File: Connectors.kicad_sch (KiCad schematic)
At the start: 20 parts, among them J2 Conn_01x08_Male, J3 Conn_01x08_Male, J4 Conn_01x08_Male, J5 5V, J6 USB_C_Receptacle_USB2.0, U15 TPD4E02B04DQA

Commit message: плата практически готова
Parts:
- removed D?: D_Schottky, Diode_SMD:D_0603_1608Metric, symbol Device:D_Schottky
- J6: footprint (none) -> Connector_USB:USB_C_Receptacle_HRO_TYPE-C-31-M-12; Manufacturer_Part_Number (none) -> 918-418K2023S40001
- STM_DEBUG1: footprint Connector:Tag-Connect_TC2030-IDC-NL_2x03_P1.27mm_Vertical -> Connector:debug_port
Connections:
- net STM_DEBUG.SWCLK: now also STM_DEBUG1.4 (Pin_4); no longer STM_DEBUG1.5 (Pin_5)
- net STM_DEBUG.SWDIO: now also STM_DEBUG1.5 (Pin_5); no longer STM_DEBUG1.4 (Pin_4)
- net USB_BOARD.DN: now also U15.1 (IO1); no longer U15.4 (IO3)
- net USB_BOARD.DP: now also U15.2 (IO2); no longer U15.5 (IO4)
- net STM_DEBUG.3V3: now reaches STM_DEBUG1.6 (Pin_6)
- net PWR_IN1 renamed PWR_IN_CONN
- net PWR_IN2 renamed VBUS
- net VBUS: now also U15.5 (IO4); no longer U15.1 (IO1)
- net PWR_IN3 renamed PWR_IN_JST
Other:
- note added: "PWR"
- note added: "USB"
- moved on the sheet: J2, J3, J4, J5, J6, R38, R39, U15

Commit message: продам гараж
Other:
- moved on the sheet: CAM0, CAM1, J2, J3, J4, J5, LASER1, LED1, TELEM1, TELEM2

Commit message: )
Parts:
- removed LED1: Conn_01x03_Male, Connector_PinHeader_2.54mm:PinHeader_1x03_P2.54mm_Vertical, symbol Connector:Conn_01x03_Male
- added GND, LED: Conn_01x01_Male, TestPoint:TestPoint_Pad_D2.0mm, symbol Connector:Conn_01x01_Male
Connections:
- net GND: now also GND.1 (Pin_1)
- net RPI_GPIO21: now also LED.1 (Pin_1)
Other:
- moved on the sheet: J5, J6, POWER1, R38, R39, STM_DEBUG1, U15

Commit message: тестирование
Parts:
- GND1: renamed from GND; footprint TestPoint:TestPoint_Pad_D2.0mm -> TestPoint:TestPoint_Pad_D1.5mm
- LED1: renamed from LED; footprint TestPoint:TestPoint_Pad_D2.0mm -> TestPoint:TestPoint_Pad_D1.5mm
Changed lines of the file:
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@@
   (symbol (lib_id "Connector:Conn_01x01_Male") (at 149.86 106.68 0) (unit 1)
     (in_bom yes) (on_board yes)
-    (property "Reference" "LED" (id 0) (at 151.13 100.33 0))
+    (property "Reference" "LED1" (id 0) (at 151.13 100.33 0))
     (property "Value" "Conn_01x01_Male" (id 1) (at 151.13 103.1051 0))
-    (property "Footprint" "TestPoint:TestPoint_Pad_D2.0mm" (id 2) (at 149.86 106.68 0)
+    (property "Footprint" "TestPoint:TestPoint_Pad_D1.5mm" (id 2) (at 149.86 106.68 0)
       (effects (font (size 1.27 1.27)) hide)
     )
@@
   (symbol (lib_id "power:GND") (at 157.48 115.57 90) (mirror x) (unit 1)
     (in_bom yes) (on_board yes)
-    (property "Reference" "#PWR?" (id 0) (at 163.83 115.57 0)
+    (property "Reference" "#PWR0141" (id 0) (at 163.83 115.57 0)
       (effects (font (size 1.27 1.27)) hide)
     )
@@
   (symbol (lib_id "Connector:Conn_01x01_Male") (at 149.86 115.57 0) (unit 1)
     (in_bom yes) (on_board yes)
-    (property "Reference" "GND" (id 0) (at 151.13 109.22 0))
+    (property "Reference" "GND1" (id 0) (at 151.13 109.22 0))
     (property "Value" "Conn_01x01_Male" (id 1) (at 151.13 111.9951 0))
-    (property "Footprint" "TestPoint:TestPoint_Pad_D2.0mm" (id 2) (at 149.86 115.57 0)
+    (property "Footprint" "TestPoint:TestPoint_Pad_D1.5mm" (id 2) (at 149.86 115.57 0)
       (effects (font (size 1.27 1.27)) hide)
     )

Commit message: первый релиз
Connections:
- net STM_DEBUG.RX: now also STM_DEBUG1.2 (Pin_2); no longer STM_DEBUG1.3 (Pin_3)
- net STM_DEBUG.TX: now also STM_DEBUG1.3 (Pin_3); no longer STM_DEBUG1.2 (Pin_2)
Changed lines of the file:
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@@
     (effects (font (size 1.27 1.27)) (justify left bottom))
   )
-  (label "STM_DEBUG.TX" (at 25.4 127 0)
+  (label "STM_DEBUG.TX" (at 25.4 124.46 0)
     (effects (font (size 1.27 1.27)) (justify left bottom))
   )
@@
     (effects (font (size 1.27 1.27)) (justify left bottom))
   )
-  (label "STM_DEBUG.RX" (at 25.4 124.46 0)
+  (label "STM_DEBUG.RX" (at 25.4 127 0)
     (effects (font (size 1.27 1.27)) (justify left bottom))
   )

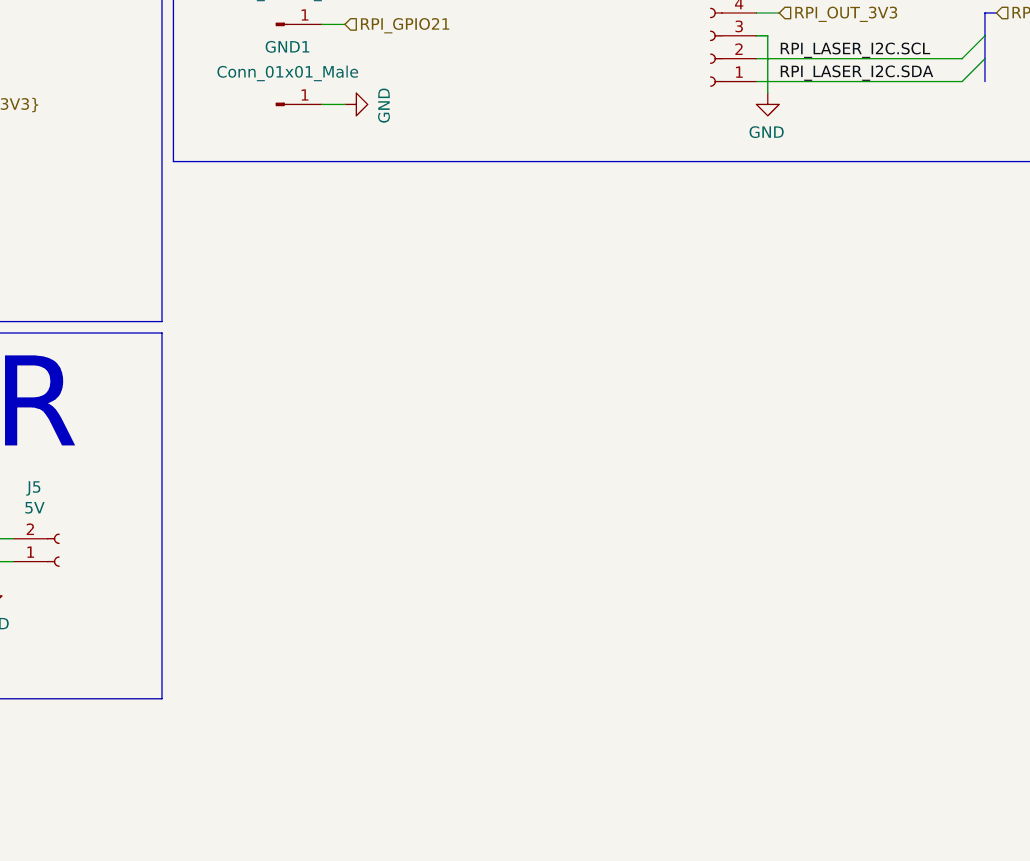
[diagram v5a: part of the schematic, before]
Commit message: Adding esp32 gpio pins
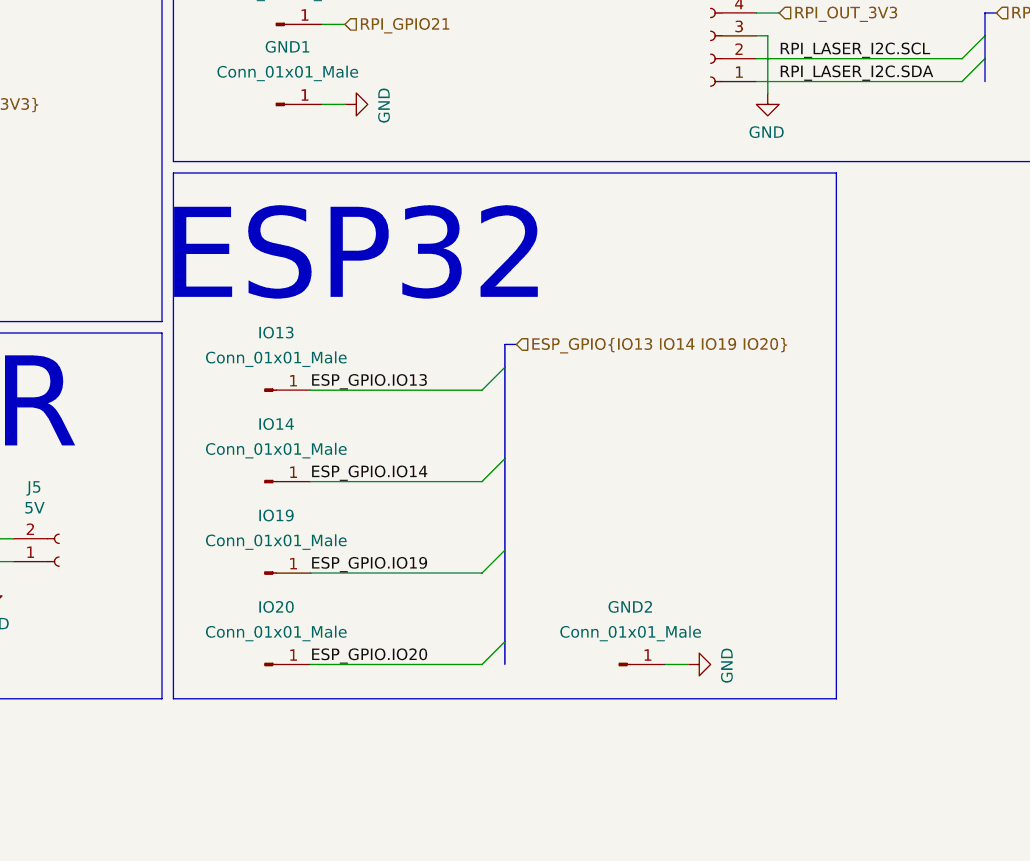
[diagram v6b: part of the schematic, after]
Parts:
- added GND2, IO13, IO14, IO19, IO20: Conn_01x01_Male, TestPoint:TestPoint_Pad_D1.5mm, symbol Connector:Conn_01x01_Male
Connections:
- net GND: now also GND2.1 (Pin_1)
- new net ESP_GPIO.IO13: IO13.1 (Pin_1)
- new net ESP_GPIO.IO14: IO14.1 (Pin_1)
- new net ESP_GPIO.IO19: IO19.1 (Pin_1)
- new net ESP_GPIO.IO20: IO20.1 (Pin_1)
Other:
- note added: "ESP32"
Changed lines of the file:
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@@
+    (stroke (width 0) (type default) (color 0 0 0 0))
+  )
+  (bus_entry (at 175.26 154.94) (size -2.54 2.54)
     (stroke (width 0) (type default) (color 0 0 0 0))
   )
@@
     (stroke (width 0) (type default) (color 0 0 0 0))
   )
+  (bus_entry (at 175.26 144.78) (size -2.54 2.54)
+    (stroke (width 0) (type default) (color 0 0 0 0))
+  )
   (bus_entry (at 226.06 40.64) (size -2.54 2.54)
     (stroke (width 0) (type default) (color 0 0 0 0))
@@
     (stroke (width 0) (type default) (color 0 0 0 0))
   )
+  (bus_entry (at 175.26 175.26) (size -2.54 2.54)
+    (stroke (width 0) (type default) (color 0 0 0 0))
+  )
   (bus_entry (at 48.26 116.84) (size -2.54 2.54)
     (stroke (width 0) (type default) (color 0 0 0 0))
@@
     (stroke (width 0) (type default) (color 0 0 0 0))
   )
+  (bus_entry (at 175.26 165.1) (size -2.54 2.54)
+    (stroke (width 0) (type default) (color 0 0 0 0))
+  )
   (bus_entry (at 102.87 33.02) (size -2.54 2.54)
     (stroke (width 0) (type default) (color 0 0 0 0))
@@
     (stroke (width 0) (type default) (color 0 0 0 0))
   )
+  (wire (pts (xy 193.04 177.8) (xy 195.58 177.8))
+    (stroke (width 0) (type default) (color 0 0 0 0))
+  )
+  (bus (pts (xy 175.26 144.78) (xy 175.26 154.94))
+    (stroke (width 0) (type default) (color 0 0 0 0))
+  )
   (bus (pts (xy 226.06 40.64) (xy 226.06 35.56))
     (stroke (width 0) (type default) (color 0 0 0 0))
@@
     (stroke (width 0) (type default) (color 0 0 0 0))
   )
+  (bus (pts (xy 175.26 165.1) (xy 175.26 175.26))
+    (stroke (width 0) (type default) (color 0 0 0 0))
+  )
   (bus (pts (xy 44.45 53.34) (xy 45.72 53.34))
     (stroke (width 0) (type default) (color 0 0 0 0))
@@
     (stroke (width 0) (type default) (color 0 0 0 0))
   )
+  (bus (pts (xy 175.26 154.94) (xy 175.26 165.1))
+    (stroke (width 0) (type default) (color 0 0 0 0))
+  )
   (bus (pts (xy 226.06 76.2) (xy 227.33 76.2))
     (stroke (width 0) (type default) (color 0 0 0 0))
@@
     (stroke (width 0) (type default) (color 0 0 0 0))
   )
+  (polyline (pts (xy 138.43 123.19) (xy 138.43 181.61))
+    (stroke (width 0) (type default) (color 0 0 0 0))
+  )
   (wire (pts (xy 151.13 71.12) (xy 153.67 71.12))
     (stroke (width 0) (type default) (color 0 0 0 0))
@@
     (stroke (width 0) (type default) (color 0 0 0 0))
   )
+  (polyline (pts (xy 212.09 181.61) (xy 212.09 123.19))
+    (stroke (width 0) (type default) (color 0 0 0 0))
+  )
   (polyline (pts (xy 12.7 139.7) (xy 12.7 12.7))
     (stroke (width 0) (type default) (color 0 0 0 0))
@@
     (stroke (width 0) (type default) (color 0 0 0 0))
   )
+  (polyline (pts (xy 212.09 123.19) (xy 138.43 123.19))
+    (stroke (width 0) (type default) (color 0 0 0 0))
+  )
   (polyline (pts (xy 138.43 121.92) (xy 251.46 121.92))
     (stroke (width 0) (type default) (color 0 0 0 0))
@@
     (stroke (width 0) (type default) (color 0 0 0 0))
   )
+  (bus (pts (xy 175.26 142.24) (xy 175.26 144.78))
+    (stroke (width 0) (type default) (color 0 0 0 0))
+  )
   (bus (pts (xy 114.3 92.71) (xy 114.3 95.25))
     (stroke (width 0) (type default) (color 0 0 0 0))
   )
+  (bus (pts (xy 176.53 142.24) (xy 175.26 142.24))
+    (stroke (width 0) (type default) (color 0 0 0 0))
+  )
   (bus (pts (xy 48.26 111.76) (xy 49.53 111.76))
     (stroke (width 0) (type default) (color 0 0 0 0))
@@
     (stroke (width 0) (type default) (color 0 0 0 0))
   )
+  (wire (pts (xy 153.67 147.32) (xy 172.72 147.32))
+    (stroke (width 0) (type default) (color 0 0 0 0))
+  )
   (bus (pts (xy 114.3 74.93) (xy 114.3 77.47))
     (stroke (width 0) (type default) (color 0 0 0 0))
@@
     (stroke (width 0) (type default) (color 0 0 0 0))
   )
+  (wire (pts (xy 153.67 167.64) (xy 172.72 167.64))
+    (stroke (width 0) (type default) (color 0 0 0 0))
+  )
   (bus (pts (xy 173.99 50.8) (xy 173.99 48.26))
     (stroke (width 0) (type default) (color 0 0 0 0))
@@
     (stroke (width 0) (type default) (color 0 0 0 0))
   )
+  (bus (pts (xy 175.26 175.26) (xy 175.26 177.8))
+    (stroke (width 0) (type default) (color 0 0 0 0))
+  )
   (wire (pts (xy 203.2 113.03) (xy 226.06 113.03))
     (stroke (width 0) (type default) (color 0 0 0 0))
@@
     (stroke (width 0) (type default) (color 0 0 0 0))
   )
+  (polyline (pts (xy 138.43 181.61) (xy 212.09 181.61))
+    (stroke (width 0) (type default) (color 0 0 0 0))
+  )
   (bus (pts (xy 173.99 35.56) (xy 173.99 33.02))
     (stroke (width 0) (type default) (color 0 0 0 0))
@@
     (stroke (width 0) (type default) (color 0 0 0 0))
   )
+  (wire (pts (xy 153.67 177.8) (xy 172.72 177.8))
+    (stroke (width 0) (type default) (color 0 0 0 0))
+  )
   (wire (pts (xy 41.91 179.07) (xy 41.91 181.61))
     (stroke (width 0) (type default) (color 0 0 0 0))
@@
   )
   (bus (pts (xy 173.99 55.88) (xy 173.99 50.8))
+    (stroke (width 0) (type default) (color 0 0 0 0))
+  )
+  (wire (pts (xy 153.67 157.48) (xy 172.72 157.48))
     (stroke (width 0) (type default) (color 0 0 0 0))
   )
@@
     (effects (font (size 10.0076 10.0076)) (justify left bottom))
   )
+  (text "ESP32" (at 137.16 138.43 0)
+    (effects (font (size 10.0076 10.0076)) (justify left bottom))
+  )
   (text "PWR" (at 96.52 154.94 0)
     (effects (font (size 10.0076 10.0076)) (justify left bottom))
   )
+  (label "ESP_GPIO.IO20" (at 153.67 177.8 0)
+    (effects (font (size 1.27 1.27)) (justify left bottom))
+  )
   (label "STM_ESC.CH8" (at 99.06 97.79 0)
     (effects (font (size 1.27 1.27)) (justify left bottom))
@@
     (effects (font (size 1.27 1.27)) (justify left bottom))
   )
+  (label "ESP_GPIO.IO14" (at 153.67 157.48 0)
+    (effects (font (size 1.27 1.27)) (justify left bottom))
+  )
   (label "STM_USART1.TX" (at 25.4 87.63 0)
     (effects (font (size 1.27 1.27)) (justify left bottom))
@@
     (effects (font (size 1.27 1.27)) (justify left bottom))
   )
+  (label "ESP_GPIO.IO19" (at 153.67 167.64 0)
+    (effects (font (size 1.27 1.27)) (justify left bottom))
+  )
   (label "STM_ESC.CH5" (at 99.06 90.17 0)
     (effects (font (size 1.27 1.27)) (justify left bottom))
@@
   )
   (label "STM_ESC.CH3" (at 99.06 85.09 0)
+    (effects (font (size 1.27 1.27)) (justify left bottom))
+  )
+  (label "ESP_GPIO.IO13" (at 153.67 147.32 0)
     (effects (font (size 1.27 1.27)) (justify left bottom))
   )
@@
   )
   (hierarchical_label "RPI_CAM0{CSI}" (shape input) (at 175.26 30.48 0)
+    (effects (font (size 1.27 1.27)) (justify left))
+  )
+  (hierarchical_label "ESP_GPIO{IO13 IO14 IO19 IO20}" (shape input) (at 176.53 142.24 0)
     (effects (font (size 1.27 1.27)) (justify left))
   )
@@
     (pin "2")
   )
+  (symbol (lib_id "Connector:Conn_01x01_Male") (at 148.59 157.48 0) (unit 1)
+    (in_bom yes) (on_board yes)
+    (property "Reference" "IO14" (id 0) (at 149.86 151.13 0))
+    (property "Value" "Conn_01x01_Male" (id 1) (at 149.86 153.9051 0))
+    (property "Footprint" "TestPoint:TestPoint_Pad_D1.5mm" (id 2) (at 148.59 157.48 0)
+      (effects (font (size 1.27 1.27)) hide)
+    )
+    (property "Datasheet" "~" (id 3) (at 148.59 157.48 0)
+      (effects (font (size 1.27 1.27)) hide)
+    )
+    (pin "1")
+  )
   (symbol (lib_id "Connector:USB_C_Receptacle_USB2.0") (at 26.67 181.61 0) (unit 1)
     (in_bom yes) (on_board yes) (fields_autoplaced)
@@
     (pin "S1")
   )
+  (symbol (lib_id "Connector:Conn_01x01_Male") (at 187.96 177.8 0) (unit 1)
+    (in_bom yes) (on_board yes)
+    (property "Reference" "GND2" (id 0) (at 189.23 171.45 0))
+    (property "Value" "Conn_01x01_Male" (id 1) (at 189.23 174.2251 0))
+    (property "Footprint" "TestPoint:TestPoint_Pad_D1.5mm" (id 2) (at 187.96 177.8 0)
+      (effects (font (size 1.27 1.27)) hide)
+    )
+    (property "Datasheet" "~" (id 3) (at 187.96 177.8 0)
+      (effects (font (size 1.27 1.27)) hide)
+    )
+    (pin "1")
+  )
+  (symbol (lib_id "Connector:Conn_01x01_Male") (at 148.59 147.32 0) (unit 1)
+    (in_bom yes) (on_board yes)
+    (property "Reference" "IO13" (id 0) (at 149.86 140.97 0))
+    (property "Value" "Conn_01x01_Male" (id 1) (at 149.86 143.7451 0))
+    (property "Footprint" "TestPoint:TestPoint_Pad_D1.5mm" (id 2) (at 148.59 147.32 0)
+      (effects (font (size 1.27 1.27)) hide)
+    )
+    (property "Datasheet" "~" (id 3) (at 148.59 147.32 0)
+      (effects (font (size 1.27 1.27)) hide)
+    )
+    (pin "1")
+  )
+  (symbol (lib_id "power:GND") (at 195.58 177.8 90) (mirror x) (unit 1)
+    (in_bom yes) (on_board yes)
+    (property "Reference" "#PWR0166" (id 0) (at 201.93 177.8 0)
+      (effects (font (size 1.27 1.27)) hide)
+    )
+    (property "Value" "GND" (id 1) (at 199.9742 177.927 0))
+    (property "Footprint" "" (id 2) (at 195.58 177.8 0)
+      (effects (font (size 1.27 1.27)) hide)
+    )
+    (property "Datasheet" "" (id 3) (at 195.58 177.8 0)
+      (effects (font (size 1.27 1.27)) hide)
+    )
+    (pin "1")
+  )
+  (symbol (lib_id "Connector:Conn_01x01_Male") (at 148.59 167.64 0) (unit 1)
+    (in_bom yes) (on_board yes)
+    (property "Reference" "IO19" (id 0) (at 149.86 161.29 0))
+    (property "Value" "Conn_01x01_Male" (id 1) (at 149.86 164.0651 0))
+    (property "Footprint" "TestPoint:TestPoint_Pad_D1.5mm" (id 2) (at 148.59 167.64 0)
+      (effects (font (size 1.27 1.27)) hide)
+    )
+    (property "Datasheet" "~" (id 3) (at 148.59 167.64 0)
+      (effects (font (size 1.27 1.27)) hide)
+    )
+    (pin "1")
+  )
+  (symbol (lib_id "Connector:Conn_01x01_Male") (at 148.59 177.8 0) (unit 1)
+    (in_bom yes) (on_board yes)
+    (property "Reference" "IO20" (id 0) (at 149.86 171.45 0))
+    (property "Value" "Conn_01x01_Male" (id 1) (at 149.86 174.2251 0))
+    (property "Footprint" "TestPoint:TestPoint_Pad_D1.5mm" (id 2) (at 148.59 177.8 0)
+      (effects (font (size 1.27 1.27)) hide)
+    )
+    (property "Datasheet" "~" (id 3) (at 148.59 177.8 0)
+      (effects (font (size 1.27 1.27)) hide)
+    )
+    (pin "1")
+  )
   (symbol (lib_id "power:GND") (at 118.11 168.91 0) (unit 1)

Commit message: Little fix
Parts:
- R38, R39: Manufacturer_Part_Number (none) -> 0402WGF5101TCE
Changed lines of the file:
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@@
+      (effects (font (size 1.27 1.27)) hide)
+    )
+    (property "Manufacturer_Part_Number" "0402WGF5101TCE" (id 4) (at 44.45 203.2 0)
       (effects (font (size 1.27 1.27)) hide)
     )
@@
       (effects (font (size 1.27 1.27)) hide)
     )
+    (property "Manufacturer_Part_Number" "0402WGF5101TCE" (id 4) (at 46.99 203.2 0)
+      (effects (font (size 1.27 1.27)) hide)
+    )

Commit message: First order
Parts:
- J5: Manufacturer_Part_Number XT30U-M -> (none)
- R38, R39: Manufacturer_Part_Number 0402WGF5101TCE -> PTFR0402B5K10N9
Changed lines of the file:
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@@
       (effects (font (size 1.27 1.27)) hide)
     )
-    (property "Manufacturer_Part_Number" "0402WGF5101TCE" (id 4) (at 44.45 203.2 0)
+    (property "Manufacturer_Part_Number" "PTFR0402B5K10N9" (id 4) (at 44.45 203.2 0)
       (effects (font (size 1.27 1.27)) hide)
     )
@@
       (effects (font (size 1.27 1.27)) hide)
     )
-    (property "Manufacturer_Part_Number" "0402WGF5101TCE" (id 4) (at 46.99 203.2 0)
+    (property "Manufacturer_Part_Number" "PTFR0402B5K10N9" (id 4) (at 46.99 203.2 0)
       (effects (font (size 1.27 1.27)) hide)
     )
@@
       (effects (font (size 1.27 1.27)) hide)
     )
-    (property "Manufacturer_Part_Number" "XT30U-M" (id 4) (at 125.73 166.37 0)
-      (effects (font (size 1.27 1.27)) hide)
-    )
